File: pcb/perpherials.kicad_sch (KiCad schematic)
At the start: 7 parts, among them J4 050700622, U1 BNO055, U6 CAT24Cxx

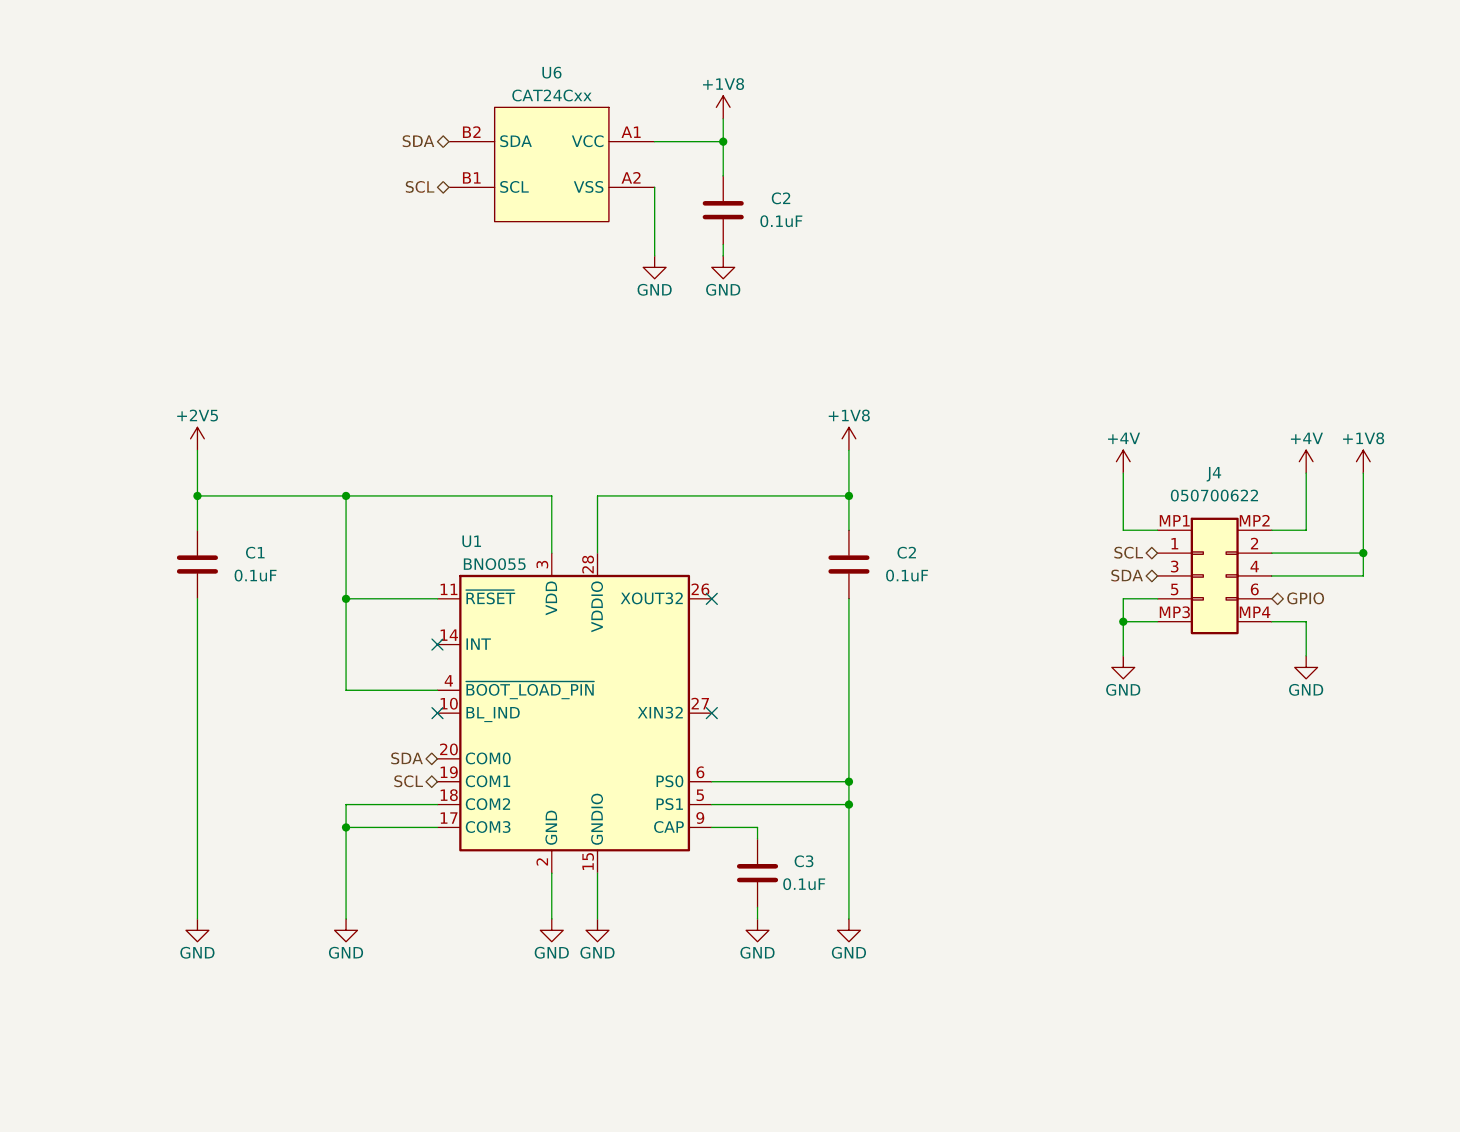
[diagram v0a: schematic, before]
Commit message: Inital routing complete
- Addressed Aaron's review
- Pullup on output side of analog switch to prevent floating SDA
- Other minor changes
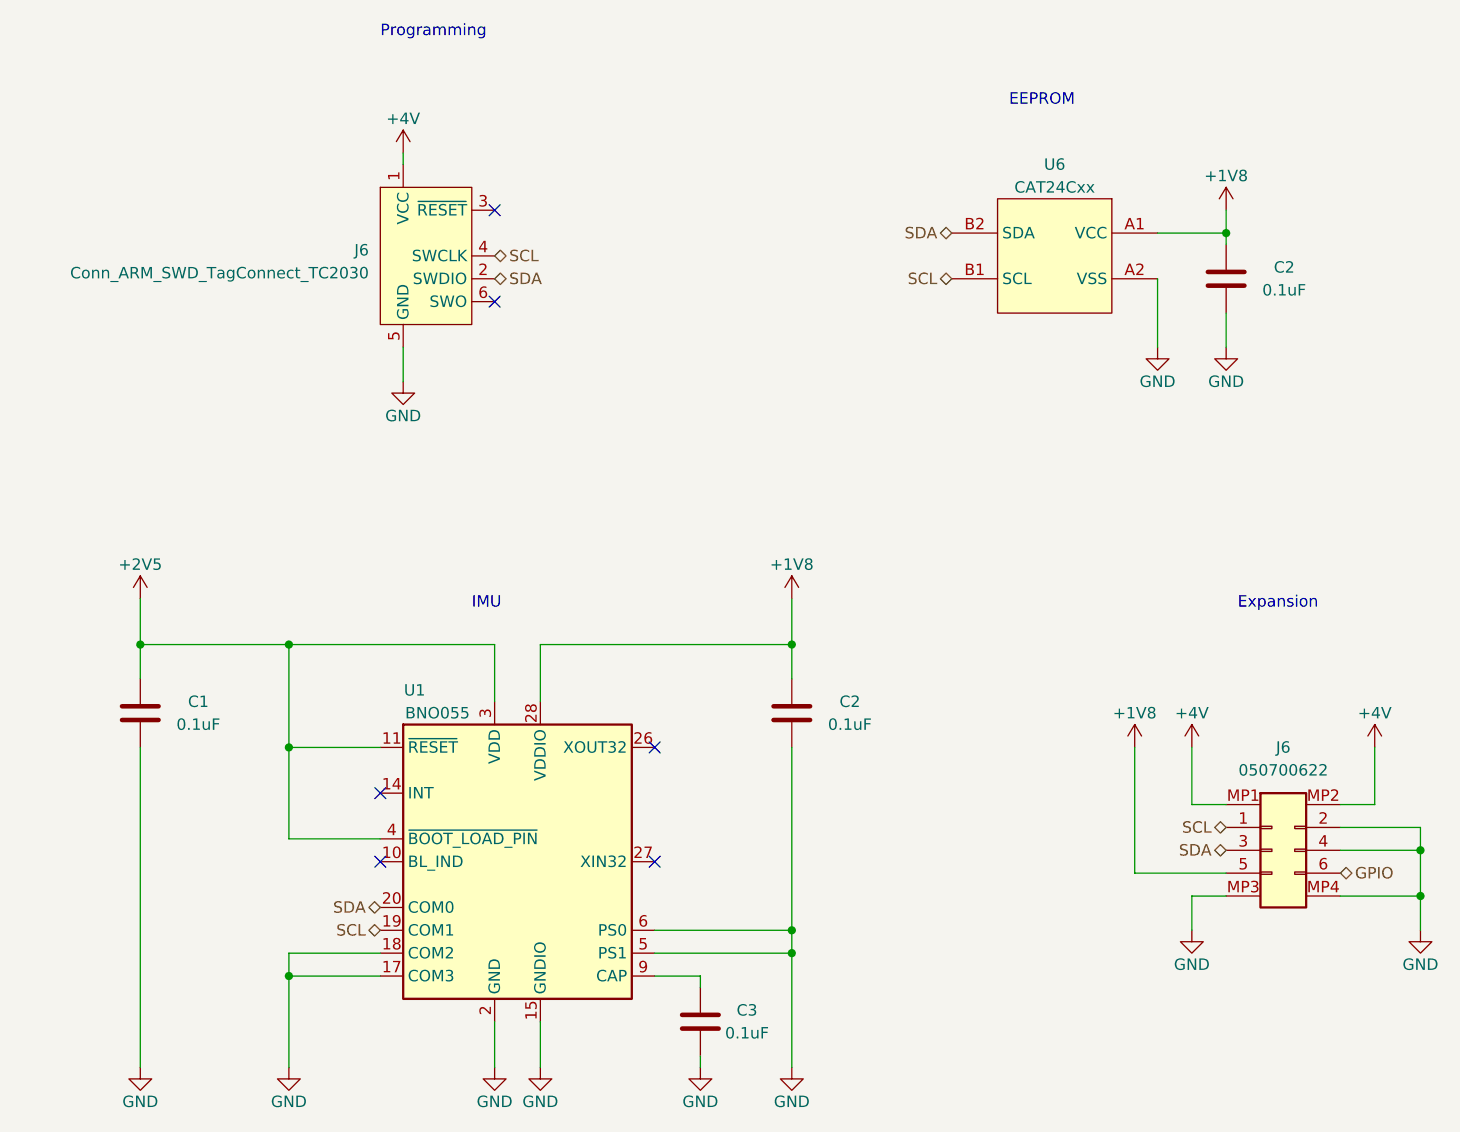
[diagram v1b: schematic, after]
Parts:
- added J6: Conn_ARM_SWD_TagConnect_TC2030, Connector:Tag-Connect_TC2030-IDC-FP_2x03_P1.27mm_Vertical, symbol Connector:Conn_ARM_SWD_TagConnect_TC2030
- renumbered J4 to J6
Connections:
- net +1V8: now also J6.5 (Pin_5); no longer J6.2 (Pin_2), J6.4 (Pin_4)
- net +4V: now also J6.1 (VCC)
- net GND: now also J6.2 (Pin_2), J6.4 (Pin_4), J6.5 (GND); no longer J6.5 (Pin_5)
- net SCL: now also J6.4 (SWCLK)
- net SDA: now also J6.2 (SWDIO)
- no-connect marks 4 -> 6
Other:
- note added: "EEPROM"
- note added: "Expansion"
- note added: "IMU"
- note added: "Programming"
- moved on the sheet: C1, C2, C3, J6, U1, U6

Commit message: Address team comments
- Add extra mouse-bite supports
- Enbiggen cable strain relief spear
- Add DNP 0.1" header for bench debug
- Small routing changes
- Update and complete BOM
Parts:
- removed J6: Conn_ARM_SWD_TagConnect_TC2030, Connector:Tag-Connect_TC2030-IDC-FP_2x03_P1.27mm_Vertical, symbol Connector:Conn_ARM_SWD_TagConnect_TC2030
- added J4: TC2030, Connector:Tag-Connect_TC2030-IDC-FP_2x03_P1.27mm_Vertical, symbol Connector:Conn_ARM_SWD_TagConnect_TC2030
- added J6: SBH11-PBPC-D05-ST-BK, Connector_IDC:IDC-Header_2x05_P2.54mm_Vertical, symbol Connector_Generic:Conn_02x05_Odd_Even
- C25, C27: renamed from C2; CASE/PACKAGE (none) -> 0201; Voltage 16V -> 25V
- C26: renamed from C1; CASE/PACKAGE (none) -> 0201; Voltage 16V -> 25V
- C28: renamed from C3; CASE/PACKAGE (none) -> 0201; Voltage 16V -> 25V
- J6: now left out of the parts list
- renumbered U1 to U7
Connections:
- net +4V: now also J4.1 (VCC), J6.1 (Pin_1), J6.2 (Pin_2)
- net GND: now also J4.5 (GND), J6.10 (Pin_10), J6.7 (Pin_7), J6.8 (Pin_8), J6.9 (Pin_9)
- net SCL: now also J4.4 (SWCLK), J6.3 (Pin_3), J6.4 (Pin_4)
- net SDA: now also J4.2 (SWDIO), J6.5 (Pin_5), J6.6 (Pin_6)
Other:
- note added: "DEBUG"
- note added: "EXPANSION"
- note added: "PROGRAMMING"
- note removed: "Expansion"
- note removed: "Programming"

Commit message: Updates to design after feedback from assembler
- Replace obsolete TE_2013496-9 ZIF connector used by IMEC with
046844727002846+, which should fit NP 2.0 flex connectors (see design
folder for comparison). We will see.
- Replaced programmable MEMS oscillator with standard quartz since this
is a common frequency.
- Other BOM updates to account for obsolete or out of stock components
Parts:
- U6: value CAT24Cxx -> CAT24C04C4ATR
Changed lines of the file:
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@@
       (effects (font (size 1.27 1.27)))
     )
-    (property "Value" "CAT24Cxx" (at 189.23 52.07 0)
+    (property "Value" "CAT24C04C4ATR" (at 189.23 52.07 0)
       (effects (font (size 1.27 1.27)))
     )
